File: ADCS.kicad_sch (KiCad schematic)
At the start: 16 parts

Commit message: ERC cleared in magnetometer connectors sheet
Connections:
- no-connect marks 4 -> 6
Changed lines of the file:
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@@
   )
   (no_connect (at 173.355 61.595))
+  (no_connect (at 226.695 99.695))
   (no_connect (at 149.86 48.26))
   (no_connect (at 173.355 59.055))
   (no_connect (at 153.035 48.26))
+  (no_connect (at 226.695 102.235))
   (wire (pts (xy 127 103.505) (xy 130.81 103.505))
     (stroke (width 0) (type default) (color 0 0 0 0))
@@
       (reference "#PWR0149") (unit 1) (value "GND") (footprint "")
     )
-    (path "/7a353e73-f362-4813-b2c3-9e73ce7ee8de/2e2e80b8-f5cb-4c8f-ae78-85b5504fc930"
+    (path "/90eea1cc-3897-47cb-b6ba-95228c17b7e0/39777bb5-1317-4037-8835-68b468778a9c"
+      (reference "#PWR0150") (unit 1) (value "GND") (footprint "")
+    )
+    (path "/90eea1cc-3897-47cb-b6ba-95228c17b7e0/930e59aa-7920-4694-ab2e-5d36d76c81e5"
+      (reference "#PWR0151") (unit 1) (value "GND") (footprint "")
+    )
+    (path "/90eea1cc-3897-47cb-b6ba-95228c17b7e0/8ddae4e6-2fb1-48ee-a7ba-c7fe49bd05fd"
+      (reference "#PWR0152") (unit 1) (value "GND") (footprint "")
+    )
+    (path "/90eea1cc-3897-47cb-b6ba-95228c17b7e0/4c6f254f-fa35-46ad-b0b5-23376efb211c"
+      (reference "#PWR0153") (unit 1) (value "GND") (footprint "")
+    )
+    (path "/90eea1cc-3897-47cb-b6ba-95228c17b7e0/b3d20957-9555-4fb2-8eaf-79bdee85bf7b"
+      (reference "#PWR0154") (unit 1) (value "GND") (footprint "")
+    )
+    (path "/90eea1cc-3897-47cb-b6ba-95228c17b7e0/4c71e0b1-249c-47cf-8dc7-0a04ae18a96b"
       (reference "#PWR0155") (unit 1) (value "GND") (footprint "")
     )
-    (path "/7a353e73-f362-4813-b2c3-9e73ce7ee8de/dd58ba90-7fd5-45b5-9c7a-d6e1781b2f1d"
+    (path "/90eea1cc-3897-47cb-b6ba-95228c17b7e0/530b147d-4a29-4a76-bcf1-5276d7edfd00"
       (reference "#PWR0156") (unit 1) (value "GND") (footprint "")
     )
-    (path "/7a353e73-f362-4813-b2c3-9e73ce7ee8de/3f8fa380-af3b-4ade-914e-d61fab940124"
+    (path "/7a353e73-f362-4813-b2c3-9e73ce7ee8de/2e2e80b8-f5cb-4c8f-ae78-85b5504fc930"
       (reference "#PWR0157") (unit 1) (value "GND") (footprint "")
     )
-    (path "/7a353e73-f362-4813-b2c3-9e73ce7ee8de/63cb63a0-ef60-4778-a586-13ded6cbed1d"
+    (path "/7a353e73-f362-4813-b2c3-9e73ce7ee8de/dd58ba90-7fd5-45b5-9c7a-d6e1781b2f1d"
       (reference "#PWR0158") (unit 1) (value "GND") (footprint "")
     )
-    (path "/7a353e73-f362-4813-b2c3-9e73ce7ee8de/df6393f7-de4a-45d3-965a-8585a86d6f54"
+    (path "/7a353e73-f362-4813-b2c3-9e73ce7ee8de/3f8fa380-af3b-4ade-914e-d61fab940124"
       (reference "#PWR0159") (unit 1) (value "GND") (footprint "")
     )
-    (path "/7a353e73-f362-4813-b2c3-9e73ce7ee8de/ee8654d1-0b53-4968-8e4c-a0ee3be7202d"
+    (path "/7a353e73-f362-4813-b2c3-9e73ce7ee8de/63cb63a0-ef60-4778-a586-13ded6cbed1d"
       (reference "#PWR0160") (unit 1) (value "GND") (footprint "")
     )
-    (path "/7a353e73-f362-4813-b2c3-9e73ce7ee8de/906c22e2-142e-466e-8b84-f99450c06396"
+    (path "/7a353e73-f362-4813-b2c3-9e73ce7ee8de/df6393f7-de4a-45d3-965a-8585a86d6f54"
       (reference "#PWR0161") (unit 1) (value "GND") (footprint "")
     )
-    (path "/7a353e73-f362-4813-b2c3-9e73ce7ee8de/f7ded9be-afd7-4da5-a8d3-9a5514b6a957"
+    (path "/7a353e73-f362-4813-b2c3-9e73ce7ee8de/ee8654d1-0b53-4968-8e4c-a0ee3be7202d"
       (reference "#PWR0162") (unit 1) (value "GND") (footprint "")
     )
-    (path "/7a353e73-f362-4813-b2c3-9e73ce7ee8de/8ce67554-98f3-4258-924e-7b3f28c8da65"
+    (path "/7a353e73-f362-4813-b2c3-9e73ce7ee8de/906c22e2-142e-466e-8b84-f99450c06396"
       (reference "#PWR0163") (unit 1) (value "GND") (footprint "")
     )
-    (path "/7a353e73-f362-4813-b2c3-9e73ce7ee8de/ebe1f3bb-28c7-47a9-905d-8a1d97af9821"
+    (path "/7a353e73-f362-4813-b2c3-9e73ce7ee8de/f7ded9be-afd7-4da5-a8d3-9a5514b6a957"
       (reference "#PWR0164") (unit 1) (value "GND") (footprint "")
     )
-    (path "/7a353e73-f362-4813-b2c3-9e73ce7ee8de/f5bc9d66-2a6d-4a54-8ce4-c18b1295443d"
+    (path "/7a353e73-f362-4813-b2c3-9e73ce7ee8de/8ce67554-98f3-4258-924e-7b3f28c8da65"
       (reference "#PWR0165") (unit 1) (value "GND") (footprint "")
     )
-    (path "/7a353e73-f362-4813-b2c3-9e73ce7ee8de/527e66a8-1f04-40e7-9652-808f66693ccb"
+    (path "/7a353e73-f362-4813-b2c3-9e73ce7ee8de/ebe1f3bb-28c7-47a9-905d-8a1d97af9821"
       (reference "#PWR0166") (unit 1) (value "GND") (footprint "")
     )
-    (path "/90eea1cc-3897-47cb-b6ba-95228c17b7e0/08c4494f-9f1c-4926-98e0-493f36ae8c45"
-      (reference "#PWR?") (unit 1) (value "GND") (footprint "")
-    )
-    (path "/90eea1cc-3897-47cb-b6ba-95228c17b7e0/1252f635-9880-4113-b5ba-9f84c80cbab9"
-      (reference "#PWR?") (unit 1) (value "GND") (footprint "")
-    )
-    (path "/90eea1cc-3897-47cb-b6ba-95228c17b7e0/35c6e339-688e-4d33-b782-0f842ecaf145"
-      (reference "#PWR?") (unit 1) (value "GND") (footprint "")
-    )
-    (path "/90eea1cc-3897-47cb-b6ba-95228c17b7e0/88ef94b4-1b3f-401a-83e5-5c6f167ecc62"
-      (reference "#PWR?") (unit 1) (value "GND") (footprint "")
-    )
-    (path "/90eea1cc-3897-47cb-b6ba-95228c17b7e0/af23a520-9df9-4aa5-a154-984e849ef1cd"
-      (reference "#PWR?") (unit 1) (value "GND") (footprint "")
-    )
-    (path "/90eea1cc-3897-47cb-b6ba-95228c17b7e0/d8b1e183-4a7e-4bfc-b021-61453d4dff31"
-      (reference "#PWR?") (unit 1) (value "GND") (footprint "")
+    (path "/7a353e73-f362-4813-b2c3-9e73ce7ee8de/f5bc9d66-2a6d-4a54-8ce4-c18b1295443d"
+      (reference "#PWR0167") (unit 1) (value "GND") (footprint "")
     )
-    (path "/90eea1cc-3897-47cb-b6ba-95228c17b7e0/fc788ebe-5dce-4622-8be8-21cfa0e0f58b"
-      (reference "#PWR?") (unit 1) (value "GND") (footprint "")
+    (path "/7a353e73-f362-4813-b2c3-9e73ce7ee8de/527e66a8-1f04-40e7-9652-808f66693ccb"
+      (reference "#PWR0168") (unit 1) (value "GND") (footprint "")
     )
     (path "/85fce53c-db5d-41a5-af86-f02ad1af70e7/c2b51706-9b59-4979-b562-badd0d98848a"
@@
     )
     (path "/7a353e73-f362-4813-b2c3-9e73ce7ee8de/c0b6aae2-d2fb-4c24-8018-c87793aa0bc5"
-      (reference "JSC2") (unit 1) (value "2367196-8") (footprint "")
+      (reference "JSC1") (unit 1) (value "2367196-8") (footprint "")
     )
     (path "/7a353e73-f362-4813-b2c3-9e73ce7ee8de/13322a77-605b-4be5-b2dd-79463d9741a1"
-      (reference "JSC3") (unit 1) (value "2367196-8") (footprint "")
+      (reference "JSC2") (unit 1) (value "2367196-8") (footprint "")
     )
     (path "/7a353e73-f362-4813-b2c3-9e73ce7ee8de/bc881d84-acb0-47e4-a4fd-7df5f6a41d2c"
-      (reference "JSC4") (unit 1) (value "2367196-8") (footprint "")
+      (reference "JSC3") (unit 1) (value "2367196-8") (footprint "")
     )
     (path "/7a353e73-f362-4813-b2c3-9e73ce7ee8de/b3d01bfb-8b47-4749-83f8-a4d3e7a7fadf"
-      (reference "JSC5") (unit 1) (value "2367196-8") (footprint "")
+      (reference "JSC4") (unit 1) (value "2367196-8") (footprint "")
     )
     (path "/7a353e73-f362-4813-b2c3-9e73ce7ee8de/01c33d21-fabd-4486-8399-3525b30b3ac6"
-      (reference "JSC6") (unit 1) (value "2367196-8") (footprint "")
+      (reference "JSC5") (unit 1) (value "2367196-8") (footprint "")
     )
     (path "/7a353e73-f362-4813-b2c3-9e73ce7ee8de/f132a363-72ec-4cce-b059-5129e9f3ebb4"
-      (reference "JSC7") (unit 1) (value "2367196-8") (footprint "")
+      (reference "JSC6") (unit 1) (value "2367196-8") (footprint "")
     )
     (path "/4d1fba12-6ef0-42d4-9064-f9f362dde9b9/8656cb07-b7b7-4825-942a-87872d0ebb27"

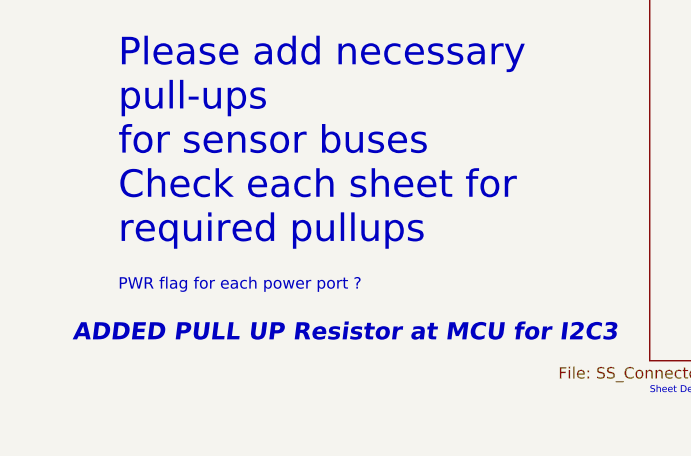
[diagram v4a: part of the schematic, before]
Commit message: Placed NCs at ADCS_HMC1051
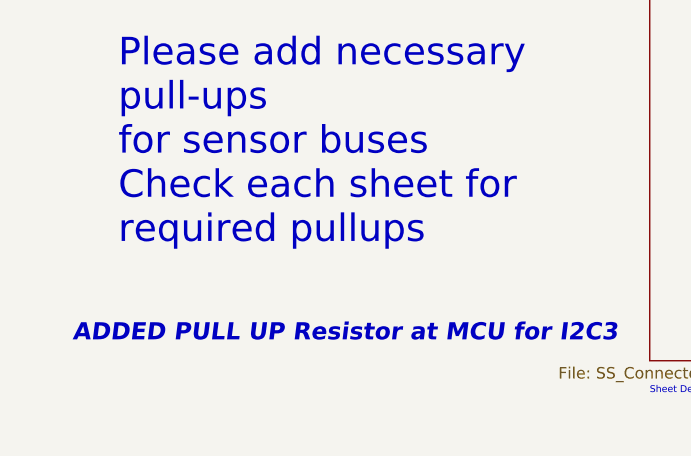
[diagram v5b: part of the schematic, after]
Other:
- note removed: "PWR flag for each power port ?"

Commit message: Page settings changed. Added some testpoints. Some comments are made.
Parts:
- removed RMCU1, RMCU2: R, symbol Device:R
- renumbered R12 to R10, R13 to R11, R14 to R12, R7 to R13, R8 to R14, R9 to R7, R10 to R8, R11 to R9
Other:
- sheet Interboard ports: added SPI2_MISO, SPI2_MOSI, SPI2_SCK; removed none
- sheet MCU ports: added SPI2_MISO, SPI2_MOSI, SPI2_SCK; removed none
- note added: "CHANGED THE I2C FROM sunsensor to I2C3 check once"
- note added: "Comments HERE:"
- note added: "TESTPOINT has 2.00mm diameter"
- note added: "What about IN_4_P & N in ADCS_HMC1051 schematic"
- note removed: "->Interboard ->I2C for aux magnetometer ->TP_fanout"
- note removed: "ADDED PULL UP Resistor at MCU for I2C3"
- note removed: "CHANGED THE I2C NAME HERE. CHECK ONCE"
- note removed: "Check this connection"
- note removed: "Fan out sensor interface for external testing"
- note removed: "LIST OF EXTERNAL INTERFACES:"
- note removed: "Please add necessary pull-ups for sensor buses Check each sheet for required pullups"
- moved on the sheet: R1, R10, R11, R12, R13, R14, R2, R3, R4, R5, R6, R7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

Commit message: FInal comments
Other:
- note added: "Chinmay: ESD Diodes"
- note added: "GGWP, Please proceed with BOM creation and uploading the schematic"
- note added: "chinmay : fanout to TP"
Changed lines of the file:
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@@
     (effects (font (size 1.27 1.27)) (justify left bottom))
+  )
+  (text "GGWP, Please proceed with BOM creation and uploading the schematic "
+    (at 127 24.13 0)
+    (effects (font (size 2.54 2.54)) (justify left bottom))
   )
   (text "Sheet Designator R\n" (at 86.995 80.645 0)
@@
     (effects (font (size 1.27 1.27)) (justify left bottom))
   )
+  (text "chinmay : fanout to TP \n" (at 20.32 243.84 0)
+    (effects (font (size 1.27 1.27)) (justify left bottom))
+  )
   (text "sheet desig G\n\n" (at 310.515 234.95 0)
     (effects (font (size 1.27 1.27)) (justify left bottom))
   )
+  (text "Chinmay: ESD Diodes\n" (at 143.51 163.83 0)
+    (effects (font (size 2.54 2.54)) (justify left bottom))
+  )
   (text "CHANGED THE I2C FROM sunsensor to I2C3\ncheck once\n"

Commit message: I2C lines are pulled up
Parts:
- added R15, R16: 0, Resistor_SMD:R_0603_1608Metric, symbol Device:R
- R1, R10, R11, R12, R13, R14, R2, R3, R4, R5, R6, R7, R8, R9: footprint (none) -> Resistor_SMD:R_0603_1608Metric
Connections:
- net I2C1_SCL: now also R15.1
- net I2C1_SDA: now also R16.1
- net I2C3_SCL: no longer R13.1
- net I2C3_SDA: no longer R14.1
- new net ADCS_HMC1051_transducer/MAG_SCL: R13.1
- new net ADCS_HMC1051_transducer/MAG_SDA: R14.1
- new net Gyro/IMU_SCL: R15.2
- new net Gyro/IMU_SDA: R16.2
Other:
- sheet Interboard ports: added SPI2_CS; removed none
- sheet MCU ports: added SPI2_CS; removed none
- note added: "Abhinav : Done"
- note removed: "Sheet designator M"
